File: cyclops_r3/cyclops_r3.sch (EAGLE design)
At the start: 133 parts, among them Q1 BC817, Q2 IRF510, U1 MCP4921, U10 TLV2374, U11 THS4281, U12 MAX4564, U13 ZXTD45, U14 ZXTD45, U2 ADG3301, U3 MCP4022-50k, U4 LT1931, U5 317-N, U6 337L, U7 TLV3701, U8 ADR03, U9 OP1177, X1 SLP3, X2 SLP3, X3 SLP3

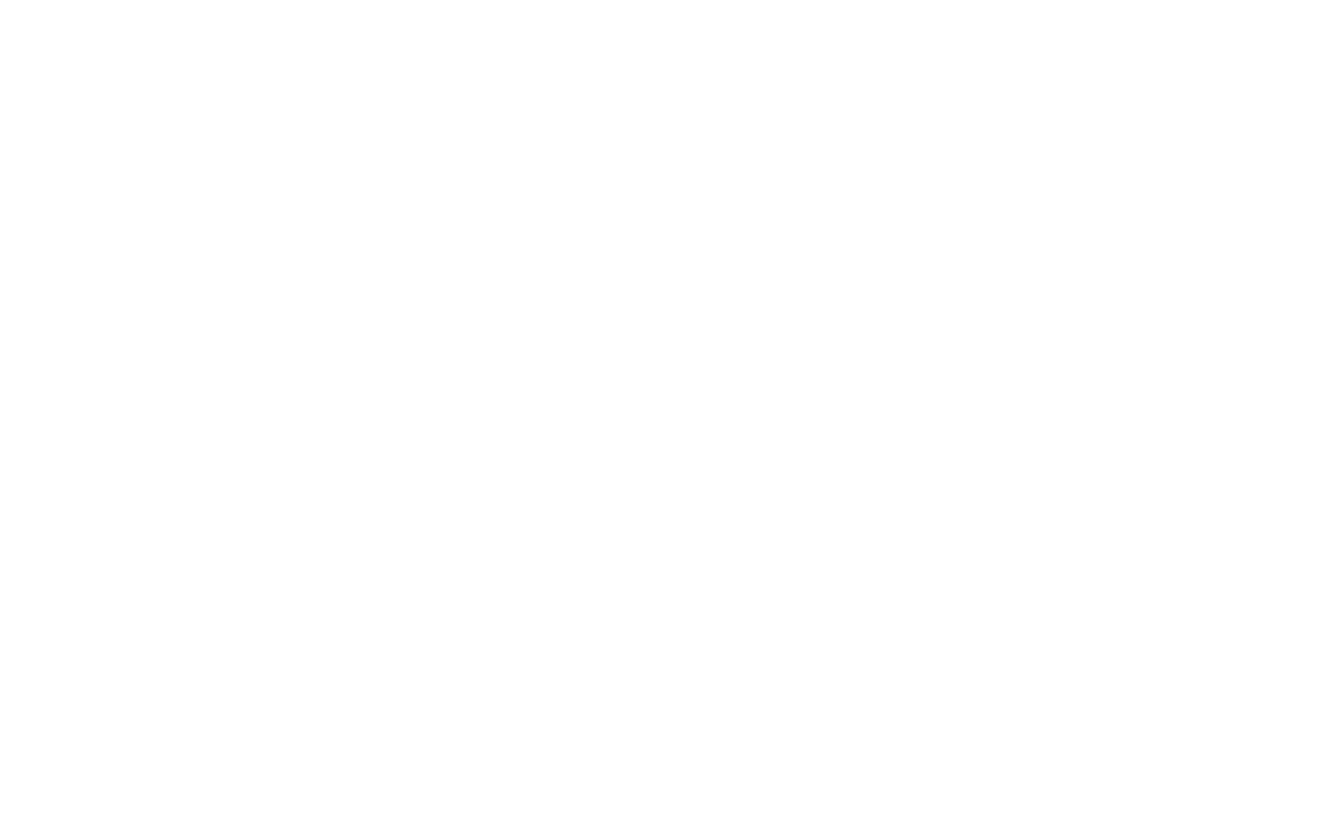
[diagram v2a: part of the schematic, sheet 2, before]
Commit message: Built the LT1963 circuit next to the LM317, I will now replace the LM317.
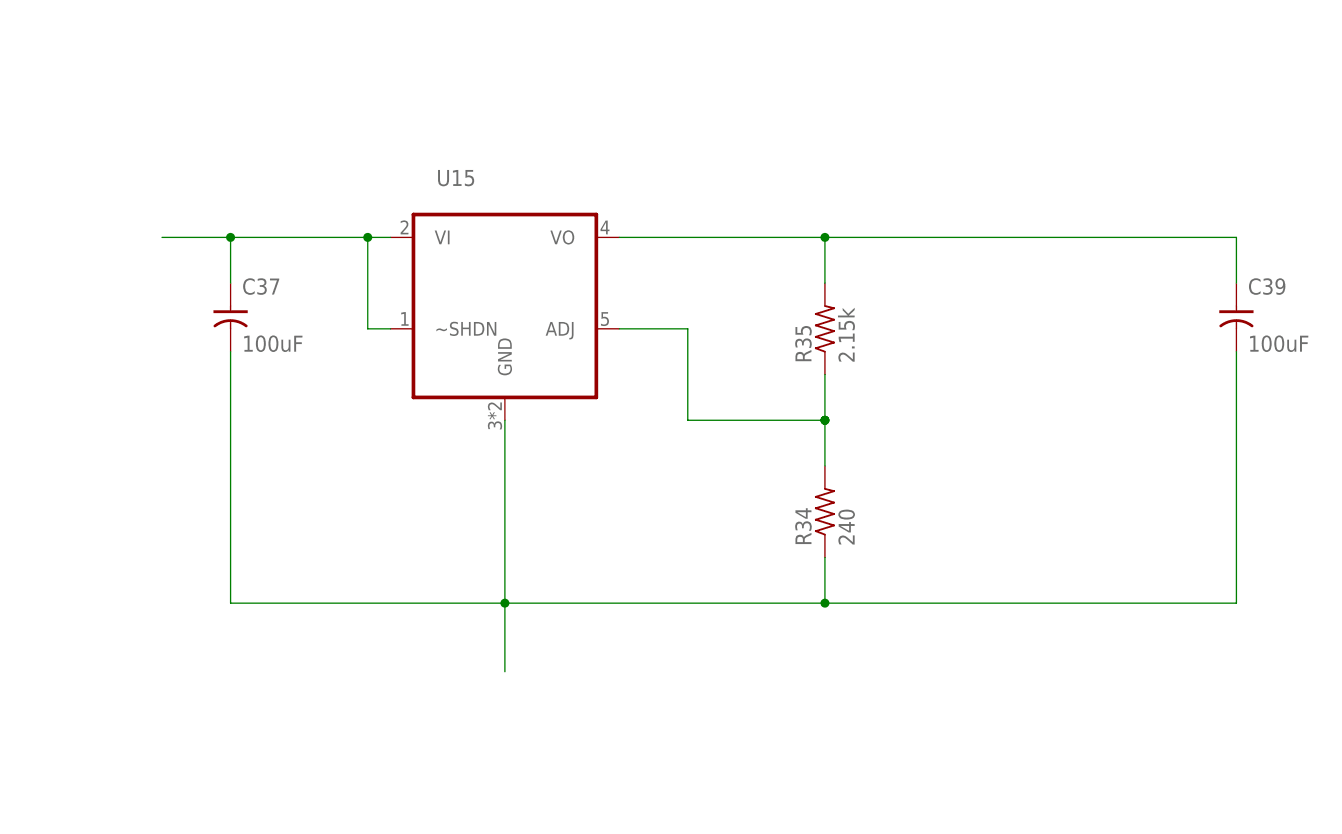
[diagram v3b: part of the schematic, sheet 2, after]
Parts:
- added C37, C39: 100uF, cyclops:C-POL_0807
- added R34: 240, cyclops:R_0603
- added R35: 2.15k, cyclops:R_0603
- added U15: (no value), cyclops:LT1963_DDPAK
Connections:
- new net +12V: C39.+, R35.2, U15.VO
- new net N$12: R34.2, R35.1, U15.ADJ
- net +15V: now also C37.+, U15.VI, U15.~SHDN
- net GND: now also C37.-, C39.-, R34.1, U15.GND
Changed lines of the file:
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@@
 <?xml version="1.0" encoding="utf-8"?>
 <!DOCTYPE eagle SYSTEM "eagle.dtd">
-<eagle version="6.5.0">
+<eagle version="6.6.0">
 <drawing>
 <settings>
@@
 <part name="U$53" library="cyclops" deviceset="GND2" device=""/>
 <part name="U$11" library="cyclops" deviceset="GND2" device=""/>
+<part name="U15" library="cyclops" deviceset="LT1963" device="_DDPAK"/>
+<part name="C37" library="cyclops" deviceset="C-POL" device="_0807" value="100uF"/>
+<part name="C39" library="cyclops" deviceset="C-POL" device="_0807" value="100uF"/>
+<part name="R34" library="cyclops" deviceset="R" device="_0603" value="240"/>
+<part name="R35" library="cyclops" deviceset="R" device="_0603" value="2.15k"/>
 </parts>
 <sheets>
@@
 <instance part="P+15" gate="1" x="-101.6" y="-66.04"/>
 <instance part="C9" gate="C" x="-78.74" y="-88.9"/>
+<instance part="U15" gate="G$1" x="210.82" y="33.02"/>
+<instance part="C37" gate="C" x="180.34" y="22.86"/>
+<instance part="C39" gate="C" x="292.1" y="22.86"/>
+<instance part="R34" gate="R" x="246.38" y="2.54" smashed="yes" rot="R90">
+<attribute name="NAME" x="244.8814" y="-1.27" size="1.778" layer="95" rot="R90"/>
+<attribute name="VALUE" x="249.682" y="-1.27" size="1.778" layer="96" rot="R90"/>
+</instance>
+<instance part="R35" gate="R" x="246.38" y="22.86" rot="R90"/>
 </instances>
 <busses>
@@
 <pinref part="C9" gate="C" pin="2"/>
 </segment>
+<segment>
+<pinref part="R34" gate="R" pin="1"/>
+<wire x1="246.38" y1="-2.54" x2="246.38" y2="-7.62" width="0.1524" layer="91"/>
+<pinref part="U15" gate="G$1" pin="GND"/>
+<wire x1="246.38" y1="-7.62" x2="210.82" y2="-7.62" width="0.1524" layer="91"/>
+<wire x1="210.82" y1="-7.62" x2="210.82" y2="12.7" width="0.1524" layer="91"/>
+<junction x="246.38" y="-7.62"/>
+<pinref part="C37" gate="C" pin="-"/>
+<wire x1="180.34" y1="20.32" x2="180.34" y2="-7.62" width="0.1524" layer="91"/>
+<wire x1="180.34" y1="-7.62" x2="210.82" y2="-7.62" width="0.1524" layer="91"/>
+<junction x="210.82" y="-7.62"/>
+<wire x1="246.38" y1="-7.62" x2="292.1" y2="-7.62" width="0.1524" layer="91"/>
+<wire x1="292.1" y1="-7.62" x2="292.1" y2="20.32" width="0.1524" layer="91"/>
+<pinref part="C39" gate="C" pin="-"/>
+<wire x1="210.82" y1="-7.62" x2="210.82" y2="-15.24" width="0.1524" layer="91"/>
+</segment>
 </net>
 <net name="N$3" class="0">
@@
 <label x="-63.5" y="35.56" size="1.778" layer="95"/>
 <wire x1="-66.04" y1="35.56" x2="-38.1" y2="35.56" width="0.1524" layer="91"/>
+</segment>
+<segment>
+<pinref part="U15" gate="G$1" pin="VI"/>
+<wire x1="198.12" y1="33.02" x2="195.58" y2="33.02" width="0.1524" layer="91"/>
+<pinref part="C37" gate="C" pin="+"/>
+<wire x1="195.58" y1="33.02" x2="180.34" y2="33.02" width="0.1524" layer="91"/>
+<wire x1="180.34" y1="33.02" x2="172.72" y2="33.02" width="0.1524" layer="91"/>
+<wire x1="180.34" y1="27.94" x2="180.34" y2="33.02" width="0.1524" layer="91"/>
+<junction x="180.34" y="33.02"/>
+<pinref part="U15" gate="G$1" pin="~SHDN"/>
+<wire x1="198.12" y1="22.86" x2="195.58" y2="22.86" width="0.1524" layer="91"/>
+<wire x1="195.58" y1="22.86" x2="195.58" y2="33.02" width="0.1524" layer="91"/>
+<junction x="195.58" y="33.02"/>
 </segment>
 </net>
@@
 </segment>
 </net>
+<net name="+12V" class="1">
+<segment>
+<pinref part="R35" gate="R" pin="2"/>
+<wire x1="246.38" y1="27.94" x2="246.38" y2="33.02" width="0.1524" layer="91"/>
+<pinref part="U15" gate="G$1" pin="VO"/>
+<wire x1="223.52" y1="33.02" x2="246.38" y2="33.02" width="0.1524" layer="91"/>
+<pinref part="C39" gate="C" pin="+"/>
+<wire x1="246.38" y1="33.02" x2="292.1" y2="33.02" width="0.1524" layer="91"/>
+<wire x1="292.1" y1="33.02" x2="292.1" y2="27.94" width="0.1524" layer="91"/>
+<junction x="246.38" y="33.02"/>
+</segment>
+</net>
+<net name="N$12" class="0">
+<segment>
+<pinref part="R34" gate="R" pin="2"/>
+<wire x1="246.38" y1="7.62" x2="246.38" y2="12.7" width="0.1524" layer="91"/>
+<junction x="246.38" y="12.7"/>
+<pinref part="R35" gate="R" pin="1"/>
+<wire x1="246.38" y1="17.78" x2="246.38" y2="12.7" width="0.1524" layer="91"/>
+<junction x="246.38" y="12.7"/>
+<wire x1="246.38" y1="12.7" x2="231.14" y2="12.7" width="0.1524" layer="91"/>
+<pinref part="U15" gate="G$1" pin="ADJ"/>
+<wire x1="223.52" y1="22.86" x2="231.14" y2="22.86" width="0.1524" layer="91"/>
+<wire x1="231.14" y1="22.86" x2="231.14" y2="12.7" width="0.1524" layer="91"/>
+</segment>
+</net>

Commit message: Started adding new linear regulator.
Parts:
- removed C10, C17: 1uF, cyclops:C-POL_1206
- removed C11: 10uF, cyclops:C-POL_1206
- removed C14, C15: 100uF, cyclops:C-POL_0807
- removed D1: S1B, cyclops:DIODES1B-13-F
- removed R7: 240, cyclops:R_0603
- removed R8: 1.87k, cyclops:R_0603
- removed U5: 317-N, cyclops:317_TO263
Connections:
- removed net +11V: AUX<>CURR.3, C14.+, C15.+, C17.+, C21.1, C22.1, C23.1, C24.1, C25.1, C27.1, C29.1, C32.1, C35.1, C36.1, D1.A, D3.C, EXPANSION.7, L2.2, Q2.D, R11.1, R14.2, R23.2, R29.1, R7.2, R9.2, U10P.V+, U11G$2.V+, U12.V+, U13.C1, U14.C1, U5.VO, U7.VCC, U8.VIN, U9.V+
- removed net N$72: C11.+, R7.1, R8.2, U5.ADJ
- net +12V: now also AUX<>CURR.3, C21.1, C22.1, C23.1, C24.1, C25.1, C27.1, C29.1, C32.1, C35.1, C36.1, D3.C, EXPANSION.7, L2.2, Q2.D, R11.1, R14.2, R23.2, R29.1, R9.2, U10P.V+, U11G$2.V+, U12.V+, U13.C1, U14.C1, U7.VCC, U8.VIN, U9.V+
- net +15V: no longer C10.+, D1.C, U5.VI
- net GND: no longer C10.-, C11.-, C14.-, C15.-, C17.-, R8.1
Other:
- moved on the sheet: C37, C39, PWR, R34, R35, R9, U15

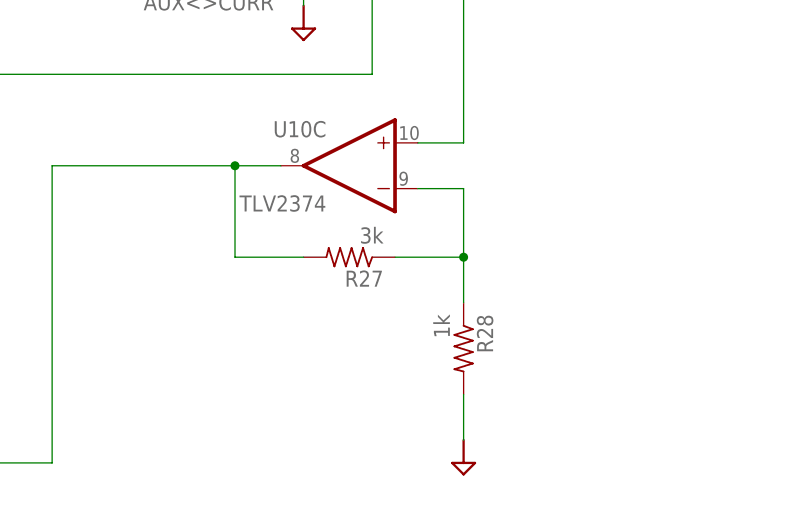
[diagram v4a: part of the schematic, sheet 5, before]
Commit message: Added LM1936 to the board.
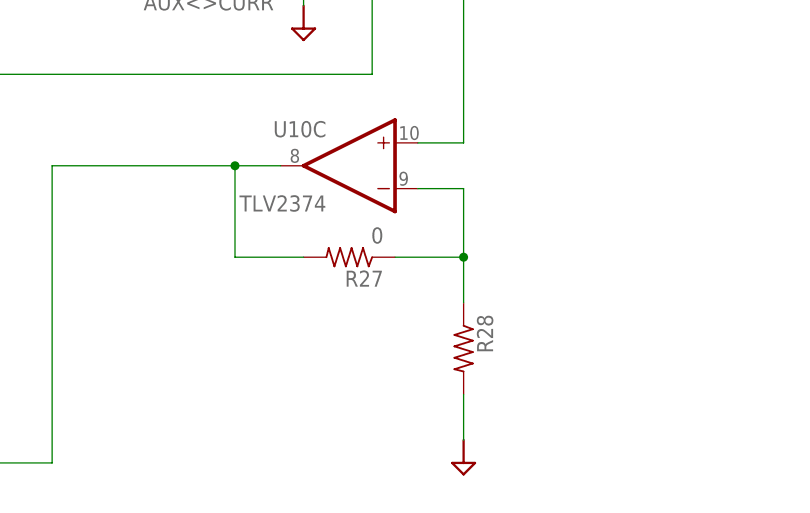
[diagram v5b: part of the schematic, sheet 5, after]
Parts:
- R27: value 3k -> 0
- R28: value 1k -> (none)
- U15: value (none) -> LT1963A
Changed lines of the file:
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@@
 <part name="C2" library="cyclops" deviceset="C" device="_0603"/>
 <part name="R4" library="cyclops" deviceset="R" device="_0603"/>
-<part name="R27" library="cyclops" deviceset="R" device="_0603" value="3k"/>
-<part name="R28" library="cyclops" deviceset="R" device="_0603" value="1k"/>
+<part name="R27" library="cyclops" deviceset="R" device="_0603" value="0"/>
+<part name="R28" library="cyclops" deviceset="R" device="_0603"/>
 <part name="RSENSE" library="cyclops" deviceset="R" device="_2512" value="1R0,2W"/>
 <part name="U8" library="cyclops" deviceset="ADR03AKSZ-REEL7" device="" value="ADR03"/>
@@
 <part name="U$53" library="cyclops" deviceset="GND2" device=""/>
 <part name="U$11" library="cyclops" deviceset="GND2" device=""/>
-<part name="U15" library="cyclops" deviceset="LT1963" device="_DDPAK"/>
+<part name="U15" library="cyclops" deviceset="LT1963" device="_DDPAK" value="LT1963A"/>
 <part name="C37" library="cyclops" deviceset="C-POL" device="_0807" value="100uF"/>
 <part name="C39" library="cyclops" deviceset="C-POL" device="_0807" value="100uF"/>

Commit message: Minor board mods. Only a couple TODOs left before fabrication.
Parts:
- added C10: 10uF, cyclops:C-POL_1206
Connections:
- net +12V: now also C10.+
- net GND: now also C10.-
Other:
- moved on the sheet: PWR, R9
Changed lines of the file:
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@@
 <part name="U$10" library="cyclops" deviceset="GND2" device=""/>
 <part name="U$58" library="cyclops" deviceset="GND2" device=""/>
+<part name="C10" library="cyclops" deviceset="C-POL" device="_1206" value="10uF"/>
 </parts>
 <sheets>
@@
 <instances>
 <instance part="FRAME2" gate="G$1" x="-109.22" y="-147.32"/>
-<instance part="R9" gate="R" x="33.02" y="17.78" rot="R90"/>
-<instance part="PWR" gate="G$1" x="33.02" y="0"/>
+<instance part="R9" gate="R" x="48.26" y="17.78" rot="R90"/>
+<instance part="PWR" gate="G$1" x="48.26" y="0"/>
 <instance part="U6" gate="A1" x="93.98" y="-109.22"/>
 <instance part="C18" gate="C" x="78.74" y="-99.06"/>
 <instance part="C19" gate="C" x="109.22" y="-99.06"/>
 <instance part="U$15" gate="G$1" x="129.54" y="-83.82"/>
-<instance part="X1" gate="G$1" x="40.64" y="2.54" rot="R270"/>
+<instance part="X1" gate="G$1" x="55.88" y="2.54" rot="R270"/>
 <instance part="U4" gate="G$1" x="-48.26" y="-88.9"/>
 <instance part="C12" gate="C" x="-7.62" y="-66.04" rot="R90"/>
@@
 <instance part="R35" gate="R" x="-2.54" y="27.94" rot="R90"/>
 <instance part="U$10" gate="G$1" x="-38.1" y="-12.7"/>
-<instance part="U$58" gate="G$1" x="33.02" y="-12.7"/>
+<instance part="U$58" gate="G$1" x="48.26" y="-12.7"/>
+<instance part="C10" gate="C" x="27.94" y="27.94"/>
 </instances>
 <busses>
@@
 <segment>
 <pinref part="PWR" gate="G$1" pin="C"/>
-<wire x1="33.02" y1="-5.08" x2="33.02" y2="-10.16" width="0.1524" layer="91"/>
+<wire x1="48.26" y1="-5.08" x2="48.26" y2="-10.16" width="0.1524" layer="91"/>
 </segment>
 <segment>
@@
 <pinref part="C39" gate="C" pin="-"/>
 <wire x1="-38.1" y1="-2.54" x2="-38.1" y2="-10.16" width="0.1524" layer="91"/>
+<pinref part="C10" gate="C" pin="-"/>
+<wire x1="27.94" y1="25.4" x2="27.94" y2="-2.54" width="0.1524" layer="91"/>
+<wire x1="27.94" y1="-2.54" x2="15.24" y2="-2.54" width="0.1524" layer="91"/>
+<junction x="15.24" y="-2.54"/>
 </segment>
 </net>
@@
 <segment>
 <pinref part="R9" gate="R" pin="1"/>
-<wire x1="33.02" y1="12.7" x2="33.02" y2="2.54" width="0.1524" layer="91"/>
+<wire x1="48.26" y1="12.7" x2="48.26" y2="2.54" width="0.1524" layer="91"/>
 <pinref part="PWR" gate="G$1" pin="A"/>
 </segment>
@@
 <wire x1="15.24" y1="38.1" x2="15.24" y2="33.02" width="0.1524" layer="91"/>
 <junction x="-2.54" y="38.1"/>
-<wire x1="33.02" y1="38.1" x2="40.64" y2="38.1" width="0.1524" layer="91"/>
+<wire x1="48.26" y1="38.1" x2="55.88" y2="38.1" width="0.1524" layer="91"/>
 <pinref part="R9" gate="R" pin="2"/>
-<wire x1="33.02" y1="22.86" x2="33.02" y2="38.1" width="0.1524" layer="91"/>
-<label x="35.56" y="38.1" size="1.778" layer="95"/>
-<wire x1="15.24" y1="38.1" x2="33.02" y2="38.1" width="0.1524" layer="91"/>
+<wire x1="48.26" y1="22.86" x2="48.26" y2="38.1" width="0.1524" layer="91"/>
+<label x="50.8" y="38.1" size="1.778" layer="95"/>
+<wire x1="15.24" y1="38.1" x2="27.94" y2="38.1" width="0.1524" layer="91"/>
 <junction x="15.24" y="38.1"/>
-<junction x="33.02" y="38.1"/>
-</segment>
-</net>
+<junction x="48.26" y="38.1"/>
+<pinref part="C10" gate="C" pin="+"/>
+<wire x1="27.94" y1="38.1" x2="48.26" y2="38.1" width="0.1524" layer="91"/>
+<wire x1="27.94" y1="33.02" x2="27.94" y2="38.1" width="0.1524" layer="91"/>
+<junction x="27.94" y="38.1"/>
+</segment>
+</net>

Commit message: Updated BOM and small layout changes. Ready to print.
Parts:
- C9: device cyclops:C_0805 -> cyclops:C_1206
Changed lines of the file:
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@@
 <?xml version="1.0" encoding="utf-8"?>
 <!DOCTYPE eagle SYSTEM "eagle.dtd">
-<eagle version="6.6.0">
+<eagle version="6.5.0">
 <drawing>
 <settings>
@@
 <part name="NEG_SUPPLY" library="cyclops" deviceset="SJ2W" device=""/>
 <part name="P+15" library="cyclops" deviceset="+5V" device="" value="+5V"/>
-<part name="C9" library="cyclops" deviceset="C" device="_0805" value="4.7uF"/>
+<part name="C9" library="cyclops" deviceset="C" device="_1206" value="4.7uF"/>
 <part name="U$9" library="cyclops" deviceset="GND2" device=""/>
 <part name="U12" library="cyclops" deviceset="MAX4564" device=""/>

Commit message: Updated gerbers. Ready to fabricate.
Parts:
- removed C35: 10uF, cyclops:C_1206
- removed C36: 10nF, cyclops:C_0603
- removed C37, C39: 100uF, cyclops:C-POL_0807
- removed D4: DS11015, cyclops:S-DIODESOD-123
- added C11: 1uF, cyclops:C_1206
- added C14: 10uF, cyclops:C-POL_1206
- added C15: 22uF, cyclops:C_1210
- added C17: 1uF, cyclops:C-POL_1206
- added D1: MBR0520L, cyclops:S-DIODESOD-123
- C10: value 10uF -> 100uF; device cyclops:C-POL_1206 -> cyclops:C-POL_0807
- C12: value 1uF -> 220pF; device cyclops:C_1206 -> cyclops:C_0603
- C13: value 220pF -> 100uF; device cyclops:C_0603 -> cyclops:C-POL_0807
- C16: value 22uF -> 1uF; device cyclops:C_1210 -> cyclops:C-POL_1206
- C18, C19: value 1uF -> .1uF; device cyclops:C-POL_1206 -> cyclops:C_0603
- C20, C21, C27, C28: value .1uF -> 1uF; device cyclops:C_0603 -> cyclops:C_0805
- C22, C23, C30: value 1uF -> .1uF; device cyclops:C_0805 -> cyclops:C_0603
- C29: value 1uF -> 10nF; device cyclops:C_0805 -> cyclops:C_0603
- C31: value 10nF -> .1uF
- C32, C33: value .1uF -> 10uF; device cyclops:C_0603 -> cyclops:C_1206
- C34: value 10uF -> 10nF; device cyclops:C_1206 -> cyclops:C_0603
- D2: value MBR0520L -> DS11015
- renumbered R34 to R8, R35 to R7, REF2.5 to REF2.1, REF5.0 to REF5.1, U15 to U5
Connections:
- net +12V: now also C13.+, C14.+, C19.1, C20.1, C30.1, C33.1, C34.1, D2.C; no longer C10.+, C24.1, C29.1, C32.1, C35.1, C36.1, C39.+, D3.C
- net +15V: now also C10.+; no longer C37.+
- net -1.25V: now also C17.-, C26.1, C29.1, C32.1; no longer C19.-, C30.1, C33.1, C34.1
- net -5V: now also C16.-; no longer C18.-
- net COMP+: now also C18.1; no longer C20.1
- net GND: now also C13.-, C14.-, C15.2, C16.+, C17.+, C18.2, C19.2, D1.C, D3.A; no longer C16.2, C18.+, C19.+, C35.2, C36.2, C37.-, C39.-, D2.C, D4.A
- net N$32: now also C11.1; no longer C12.1
- net N$33: now also C11.2, D1.A; no longer C12.2, D2.A
- net N$35: now also C12.1, C15.1; no longer C13.1, C16.1
- net N$36: now also C12.2; no longer C13.2
- net REF5.0: now also C24.1; no longer C26.1
- net _VREF: now also D2.A, D3.C; no longer D3.A, D4.C
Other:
- moved on the sheet: C10, C12, C13, C16, C22, C23, C24, C27, C28, C29, C30, C31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
